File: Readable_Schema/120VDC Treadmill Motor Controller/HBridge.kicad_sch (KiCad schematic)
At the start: 10 parts, among them J2 Motor, Q6 MUN5330DW1T1G, Q8 SMUN5230DW1T1G

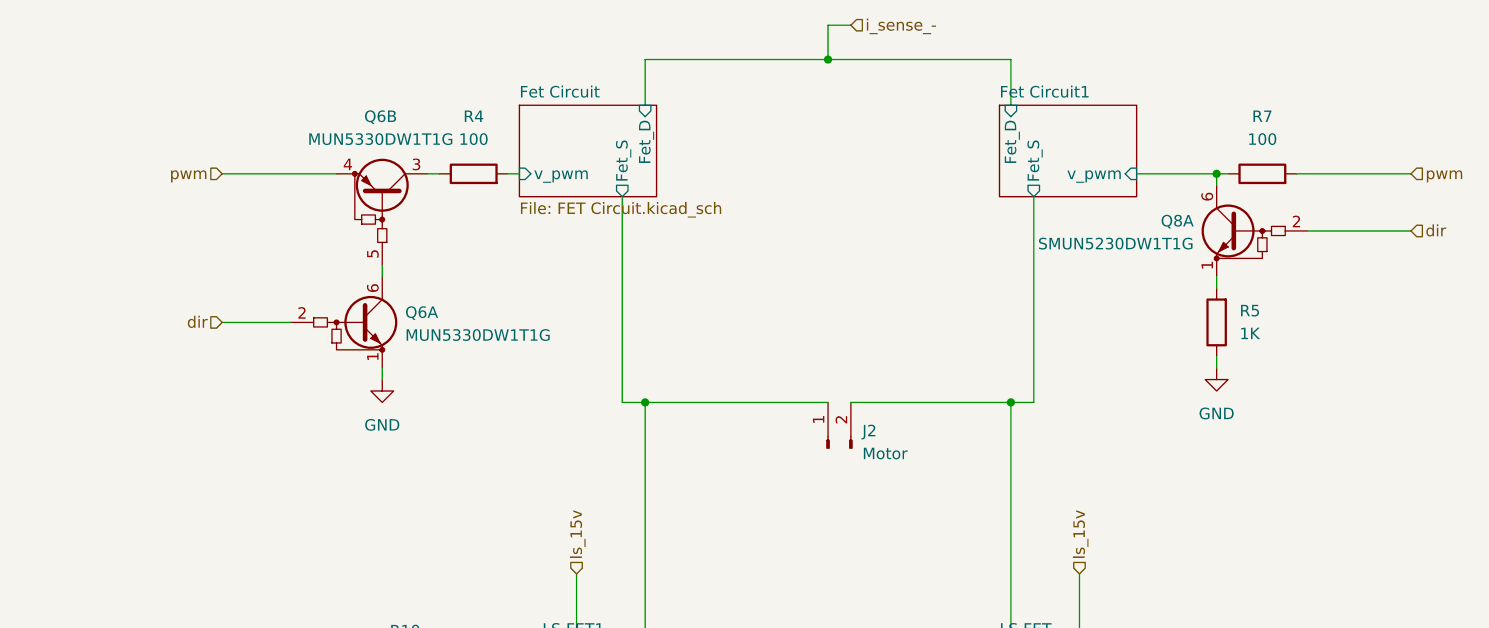
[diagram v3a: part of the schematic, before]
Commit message: Continuing to update footprints, did some follow up math on low pass filter for adc voltage coming out of current sense system
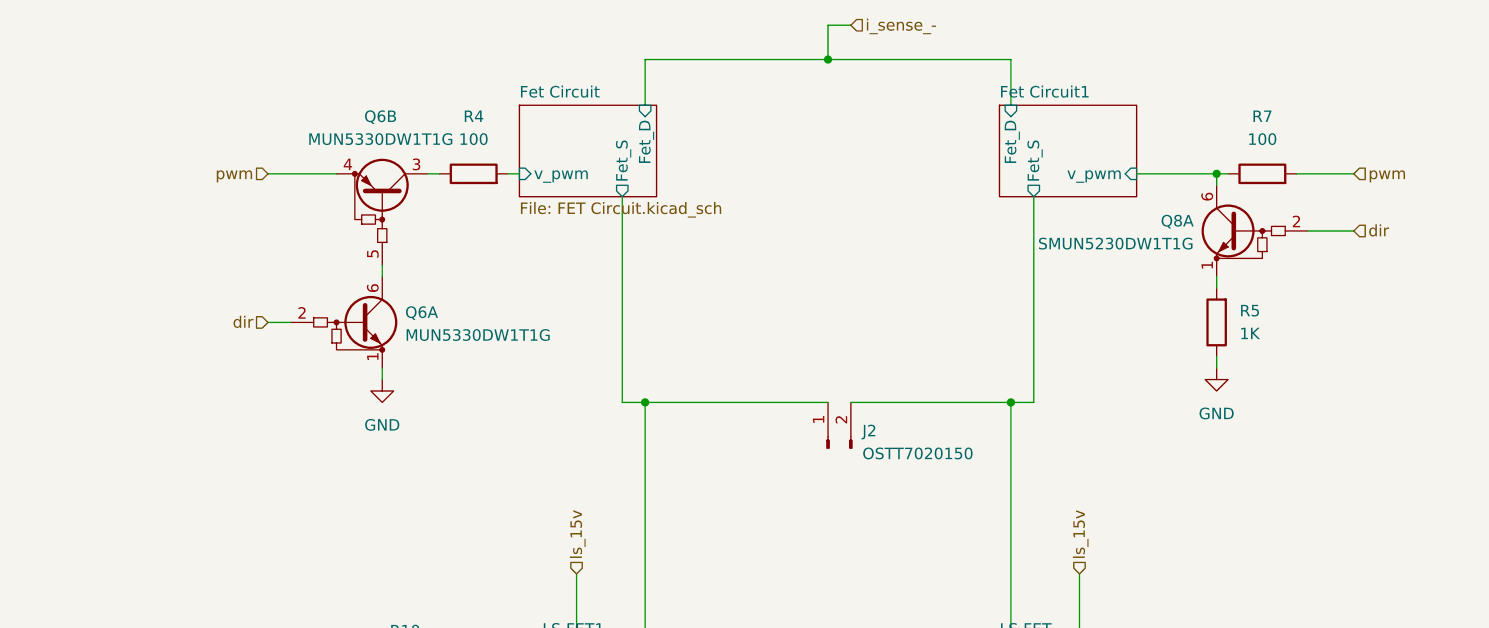
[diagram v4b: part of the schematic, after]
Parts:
- J2: value Motor -> OSTT7020150; footprint (none) -> TerminalBlock_MetzConnect:TerminalBlock_MetzConnect_Type701_RT11L02HGLU_1x02_P6.35mm_Horizontal
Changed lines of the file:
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@@
+	(wire
+		(pts
+			(xy 194.31 77.47) (xy 199.39 77.47)
+		)
+		(stroke
+			(width 0)
+			(type default)
+		)
+	)
 	(wire
 		(pts
@@
 	(wire
 		(pts
-			(xy 73.66 87.63) (xy 81.28 87.63)
+			(xy 78.74 87.63) (xy 81.28 87.63)
 		)
 		(stroke
@@
 	(wire
 		(pts
+			(xy 193.04 71.12) (xy 199.39 71.12)
+		)
+		(stroke
+			(width 0)
+			(type default)
+		)
+	)
+	(wire
+		(pts
 			(xy 118.11 134.62) (xy 118.11 142.24)
 		)
@@
 	(wire
 		(pts
-			(xy 194.31 77.47) (xy 205.74 77.47)
-		)
-		(stroke
-			(width 0)
-			(type default)
-		)
-	)
-	(wire
-		(pts
 			(xy 163.83 96.52) (xy 161.29 96.52)
 		)
@@
 	(wire
 		(pts
-			(xy 193.04 71.12) (xy 205.74 71.12)
-		)
-		(stroke
-			(width 0)
-			(type default)
-		)
-	)
-	(wire
-		(pts
 			(xy 120.65 58.42) (xy 140.97 58.42)
 		)
@@
 	(wire
 		(pts
-			(xy 73.66 71.12) (xy 86.36 71.12)
+			(xy 78.74 71.12) (xy 86.36 71.12)
 		)
 		(stroke
@@
 	(hierarchical_label "dir"
 		(shape input)
-		(at 73.66 87.63 180)
+		(at 78.74 87.63 180)
 		(effects
 			(font
@@
 	(hierarchical_label "pwm"
 		(shape input)
-		(at 73.66 71.12 180)
+		(at 78.74 71.12 180)
 		(effects
 			(font
@@
 	(hierarchical_label "dir"
 		(shape input)
-		(at 205.74 77.47 0)
+		(at 199.39 77.47 0)
 		(effects
 			(font
@@
 	(hierarchical_label "pwm"
 		(shape input)
-		(at 205.74 71.12 0)
+		(at 199.39 71.12 0)
 		(effects
 			(font
@@
 			)
 		)
-		(property "Value" "Motor"
+		(property "Value" "OSTT7020150"
 			(at 144.78 102.2349 90)
 			(effects
@@
 			)
 		)
-		(property "Footprint" ""
+		(property "Footprint" "TerminalBlock_MetzConnect:TerminalBlock_MetzConnect_Type701_RT11L02HGLU_1x02_P6.35mm_Horizontal"
 			(at 140.97 101.6 0)
 			(effects
@@
 			)
 		)
-		(property "Datasheet" "~"
+		(property "Datasheet" "https://mm.digikey.com/Volume0/opasdata/d220001/medias/docus/388/OSTT7xx0150.pdf"
 			(at 140.97 101.6 0)
 			(effects
@@
 			)
 		)
-		(property "Description" "Motor Connection"
+		(property "Description" "OSTT7020150"
 			(at 140.97 101.6 0)
 			(effects

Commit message: continued to add footprints, we still need to add hall effect circuit and possible brake resistor subcircuit. We may also want to consider switching the large 15v isolated power supplies to be smd as well as the FOD3182. Otherwise this will become a lot to hand solder.
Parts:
- J2: footprint TerminalBlock_MetzConnect:TerminalBlock_MetzConnect_Type701_RT11L02HGLU_1x02_P6.35mm_Horizontal -> Treadmill_Feet:CONN2_OSTT7020150_OST
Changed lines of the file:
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@@
 			)
 		)
-		(property "Footprint" "TerminalBlock_MetzConnect:TerminalBlock_MetzConnect_Type701_RT11L02HGLU_1x02_P6.35mm_Horizontal"
+		(property "Footprint" "Treadmill_Feet:CONN2_OSTT7020150_OST"
 			(at 140.97 101.6 0)
 			(effects

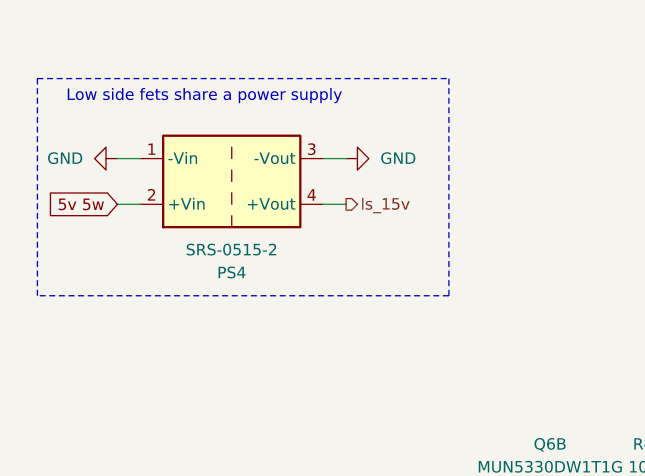
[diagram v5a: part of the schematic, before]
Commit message: -There are no power supply/ gate driver variants for the ones chosen that support smd -We NEED to workout how we want to communicate with both linuxCNC for the CNC controller and a potentiometer for the bridgeport -We NEED to incorporate a ESTOP component that directly shuts off the motor -Missing brake resistor subcircuit -Missing Input capacitors to deal with back EMF
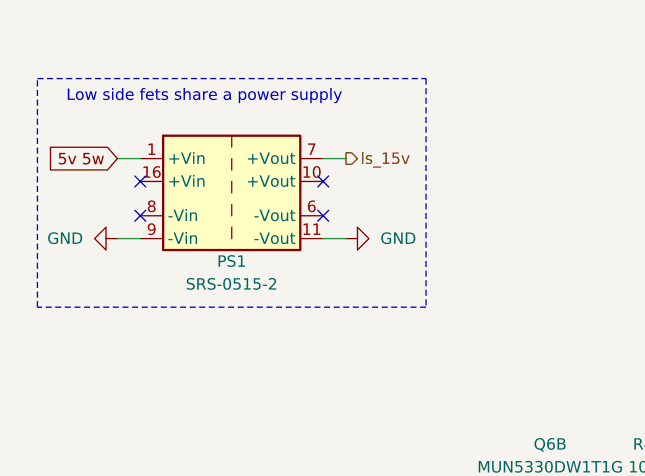
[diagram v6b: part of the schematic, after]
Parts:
- removed PS4: SRS-0515-2, Footprints_TMC:SRS-0515 DIP-16_W7.62mm, symbol Converter_DCDC:MEE1S0303SC
- added PS1: SRS-0515-2, Footprints_TMC:SRS-0515 DIP-16_W7.62mm, symbol Treadmill_Comp:SRS-0515-2
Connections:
- net 5v 5w: now also PS1.1 (+Vin)
- net GND: now also PS1.11 (-Vout), PS1.9 (-Vin)
- net ls_15v: now also PS1.7 (+Vout)
- no-connect marks 0 -> 4

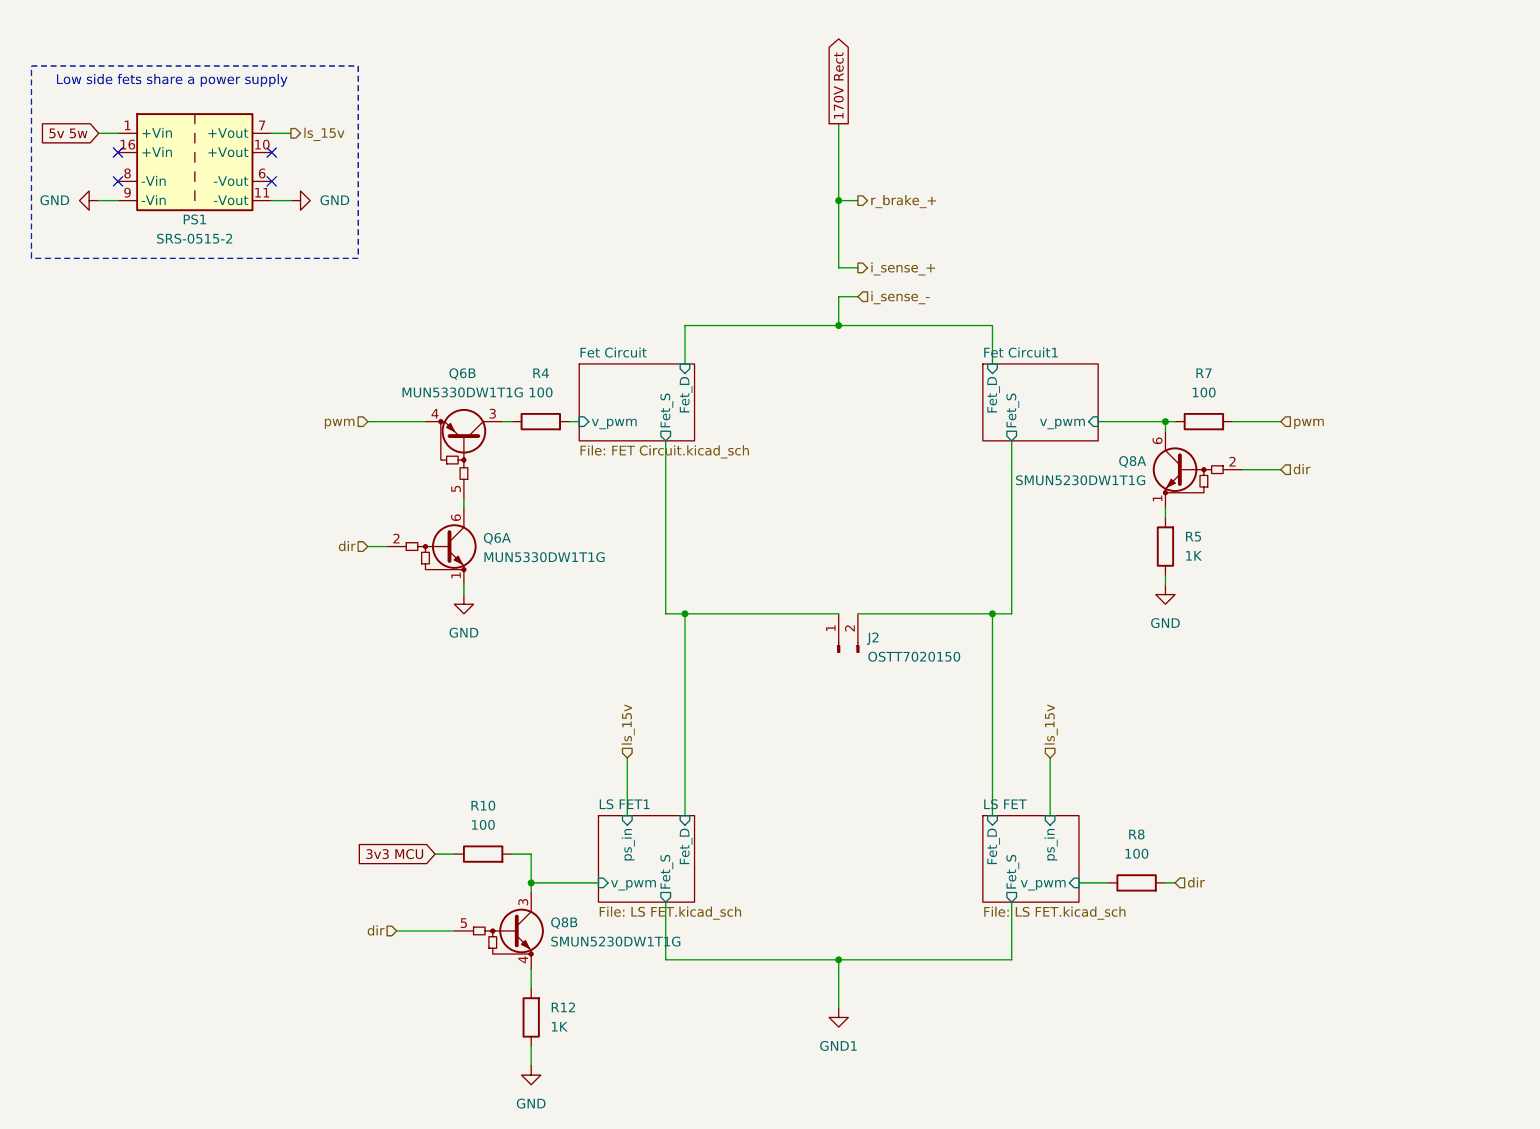
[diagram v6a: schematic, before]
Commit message: Still need to do the majority of the things mentioned in the last commit, made some progress on the mcu pinout headers, fixed a few resistors that were putting npns in a high side drive state (preventing fully grounding signal)
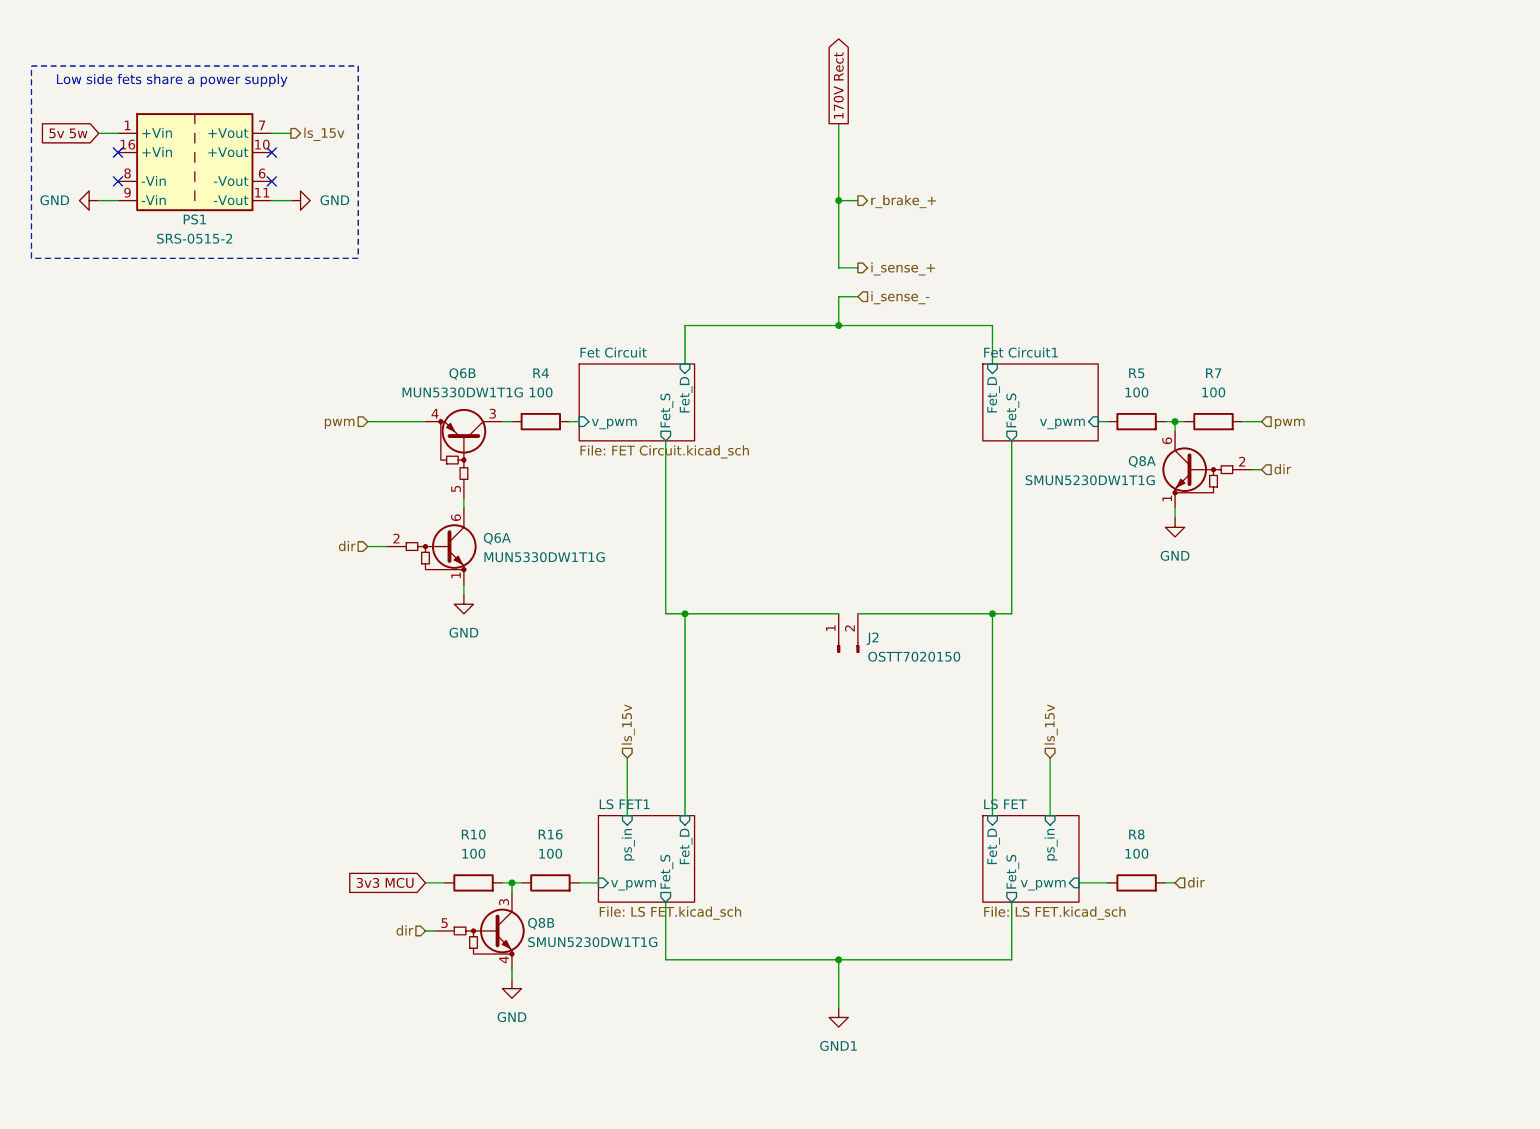
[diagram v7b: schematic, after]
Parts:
- removed R12: 1K, Resistor_SMD:R_0805_2012Metric_Pad1.20x1.40mm_HandSolder, symbol Device:R
- added R16: 100, Resistor_SMD:R_1206_3216Metric_Pad1.30x1.75mm_HandSolder, symbol Device:R
- R5: value 1K -> 100; footprint Resistor_SMD:R_0805_2012Metric_Pad1.20x1.40mm_HandSolder -> Resistor_SMD:R_1206_3216Metric_Pad1.30x1.75mm_HandSolder
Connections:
- net Fet Circuit1/v_pwm: now also R5.1; no longer Q8.6 (C1), R7.1
- net GND: now also Q8.1 (E1), Q8.4 (E2); no longer R5.1
- net LS FET1/v_pwm: now also R16.2; no longer Q8.3 (C2), R10.2
- net at R5.2: now also Q8.6 (C1), R7.1; no longer Q8.1 (E1)
- new net: Q8.3 (C2), R10.2, R16.1
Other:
- moved on the sheet: Q8A, Q8B, R10, R7
